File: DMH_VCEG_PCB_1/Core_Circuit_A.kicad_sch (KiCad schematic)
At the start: 106 parts, among them J21 Conn_01x10_PinHeader, J22 Conn_01x10_PinHeader, J24 Conn_01x06_PinHeader, Q1 BC558, Q10 BC548, Q2 BC558, Q3 BC548, Q4 BC548, Q5 MMBFJ113, Q6 MMBFJ113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

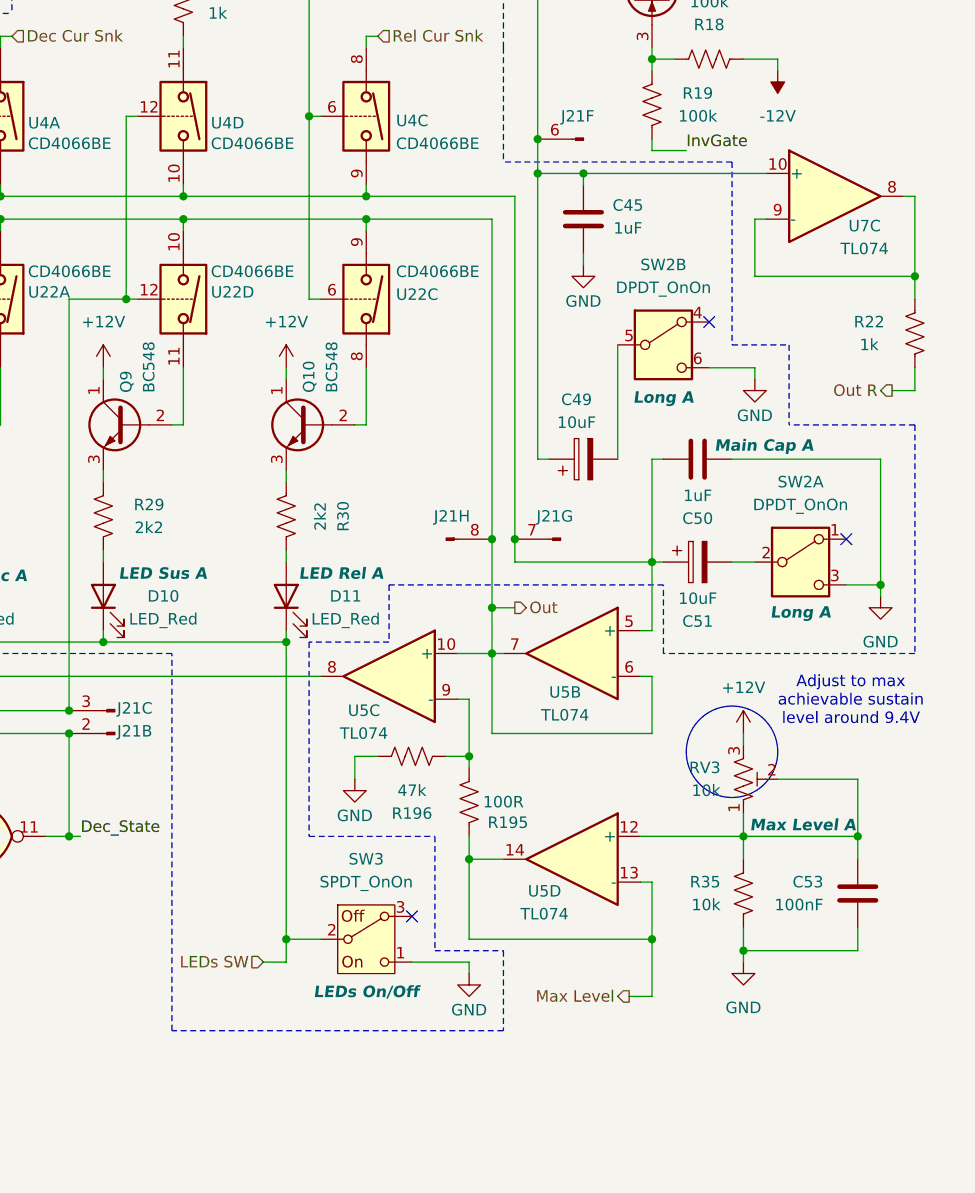
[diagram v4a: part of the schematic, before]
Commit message: Added fast cap selection
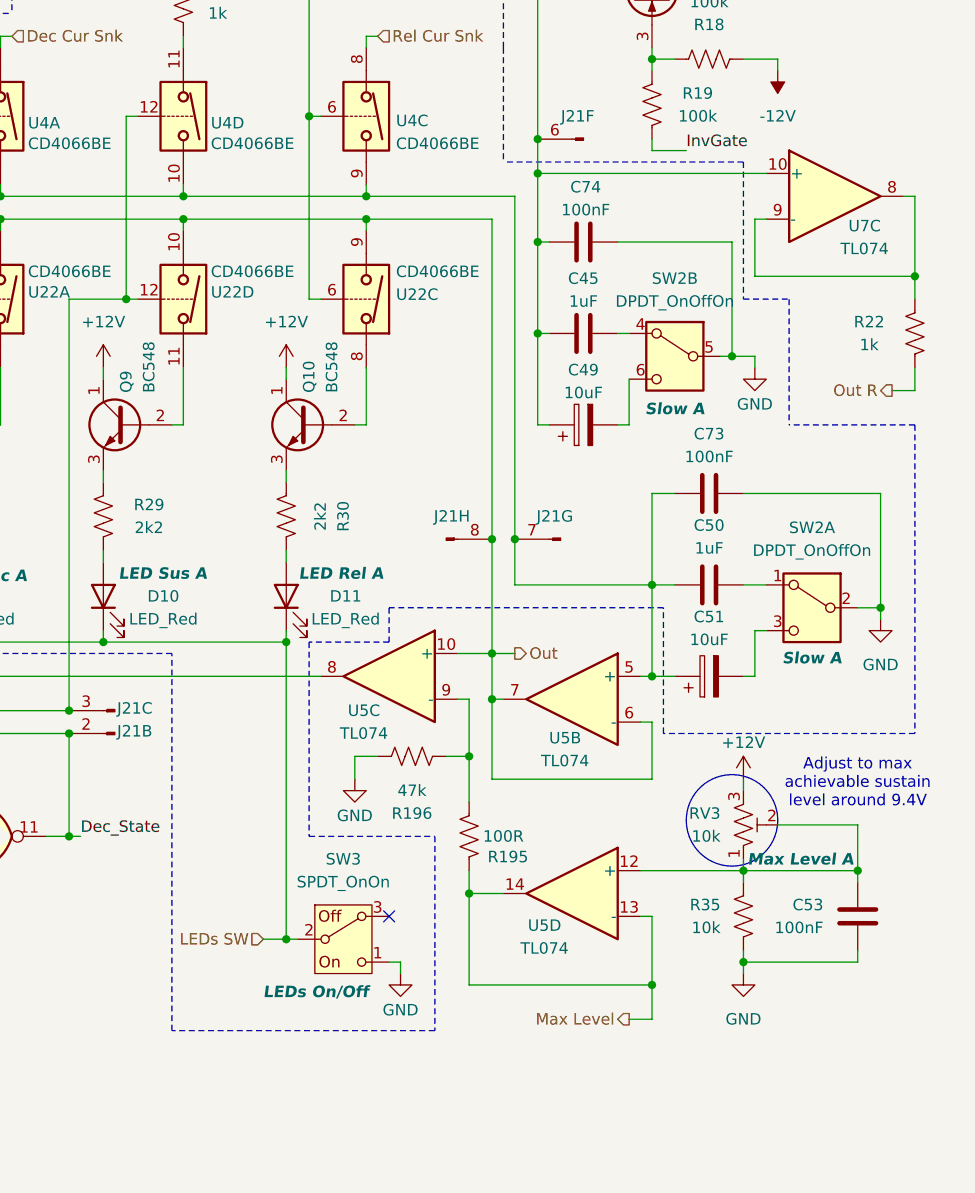
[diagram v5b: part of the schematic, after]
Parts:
- added C73, C74: 100nF, Capacitor_THT:C_Rect_L7.0mm_W4.5mm_P5.00mm, symbol Device:C
- SW2: value DPDT_OnOn -> DPDT_OnOffOn; Function Long A -> Slow A
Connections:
- net GND: now also SW2.2 (B), SW2.5 (B), C73.1, C74.1; no longer C45.1, C50.2, SW2.3 (C), SW2.6 (C)
- net at C45.2, C49.1, J21.6 (Pin_6)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: now also C74.2
- net at C51.1, J21.7 (Pin_7), U4.10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: now also C50.2, C73.2; no longer C50.1
- net at C49.2: now also SW2.6 (C); no longer SW2.5 (B)
- net at C51.2: now also SW2.3 (C); no longer SW2.2 (B)
- net at SW2.4 (A): now also C45.1
- net at SW2.1 (A): now also C50.1
- no-connect marks 5 -> 3
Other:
- moved on the sheet: C45, C49, C50, C51, C53, R195, R35, RV3, SW2A, SW2B, SW3, U5B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

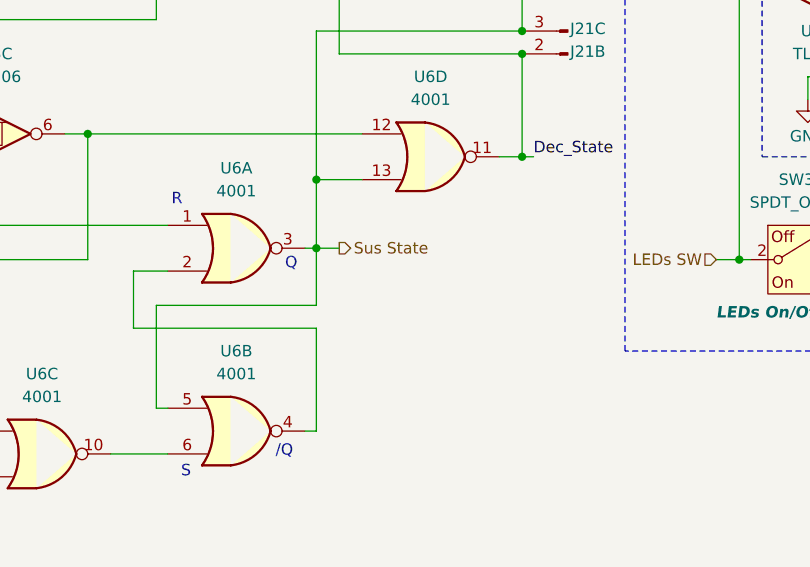
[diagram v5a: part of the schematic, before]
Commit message: Fixed Sus Gate output stage
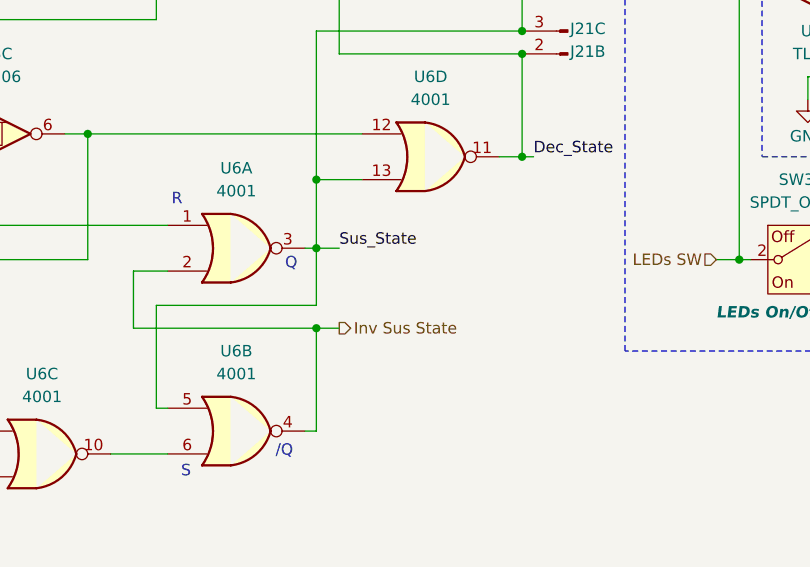
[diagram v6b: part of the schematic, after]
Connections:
- net Inv Sus State: now reaches U6.2, U6.4
- net Sus State renamed Sus_State
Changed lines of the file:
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@@
 	)
 	(junction
+		(at 166.37 162.56)
+		(diameter 0)
+		(color 0 0 0 0)
+	)
+	(junction
 		(at 110.49 86.36)
 		(diameter 0)
@@
 	(wire
 		(pts
+			(xy 166.37 162.56) (xy 168.91 162.56)
+		)
+		(stroke
+			(width 0)
+			(type default)
+		)
+	)
+	(wire
+		(pts
 			(xy 222.25 54.61) (xy 223.52 54.61)
 		)
@@
 		)
 	)
+	(label "Sus_State"
+		(at 168.91 153.67 0)
+		(effects
+			(font
+				(size 1.27 1.27)
+			)
+			(justify left bottom)
+		)
+	)
 	(hierarchical_label "Out R"
 		(shape output)
@@
 		)
 	)
-	(hierarchical_label "Sus State"
-		(shape output)
-		(at 168.91 153.67 0)
-		(effects
-			(font
-				(size 1.27 1.27)
-			)
-			(justify left)
-		)
-	)
 	(hierarchical_label "Att Cur Src"
 		(shape input)
@@
 		(effects
 			(font
+				(size 1.27 1.27)
+			)
+			(justify left)
+		)
+	)
+	(hierarchical_label "Inv Sus State"
+		(shape output)
+		(at 168.91 162.56 0)
+		(effects
+			(font

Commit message: Modified Out R
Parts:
- removed Q5, Q6: MMBFJ113, Package_TO_SOT_THT:TO-92L_Inline, symbol Transistor_FET:MMBFJ113
- removed R11, R18, R19: 100k, Resistor_THT:R_Axial_DIN0207_L6.3mm_D2.5mm_P7.62mm_Horizontal, symbol Device:R_US
- added Q5, Q6: BS170, Package_TO_SOT_THT:TO-92_Inline, symbol Transistor_FET:BS170
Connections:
- net InvGate: now also Q6.2 (G)
- net ProcGate: now also C46.1, D3.1 (K), D5.1 (K), J24.2 (Pin_2), R24.2, SW1.3 (C), U3.1, Q5.2 (G); no longer C48.2, D5.2 (A), R23.1, U1.1
- net at C45.2, C49.1, C74.2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: now also Q5.1 (D), Q6.1 (D)
- net at Q4.1 (C): now also Q6.3 (S)
- net at Q2.1 (C): now also Q5.3 (S)
- new net: C48.2, D5.2 (A), R23.1, U1.1

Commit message: Synced changes to Circuit B
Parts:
- C43: value 1nF -> 10nF
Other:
- note removed: "Was 10n"
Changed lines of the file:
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@@
 		(comment 1 "PCB for 15cm Kosmo format synthesizer module")
 	)
-	(circle
-		(center 70.612 44.196)
-		(radius 3.81)
-		(stroke
-			(width 0)
-			(type default)
-		)
-		(fill
-			(type none)
-		)
-	)
 	(rectangle
 		(start 62.23 125.73)
@@
 		)
 	)
-	(text "Was 10n"
-		(exclude_from_sim no)
-		(at 71.12 49.53 0)
-		(effects
-			(font
-				(size 1.27 1.27)
-			)
-		)
-	)
 	(text "/Q"
 		(exclude_from_sim no)
@@
 	)
 	(junction
+		(at 59.69 107.95)
+		(diameter 0)
+		(color 0 0 0 0)
+	)
+	(junction
 		(at 248.92 19.05)
 		(diameter 0)
@@
 	)
 	(junction
-		(at 59.69 104.14)
-		(diameter 0)
-		(color 0 0 0 0)
-	)
-	(junction
 		(at 222.25 74.93)
 		(diameter 0)
@@
 	(wire
 		(pts
-			(xy 59.69 107.95) (xy 59.69 104.14)
-		)
-		(stroke
-			(width 0)
-			(type default)
-		)
-	)
-	(wire
-		(pts
 			(xy 49.53 26.67) (xy 54.61 26.67)
 		)
@@
 	(wire
 		(pts
-			(xy 59.69 86.36) (xy 59.69 104.14)
-		)
-		(stroke
-			(width 0)
-			(type default)
-		)
-	)
-	(wire
-		(pts
 			(xy 120.65 140.97) (xy 123.19 140.97)
 		)
@@
 	(wire
 		(pts
-			(xy 59.69 104.14) (xy 78.74 104.14)
+			(xy 59.69 107.95) (xy 78.74 107.95)
 		)
 		(stroke
@@
 	(wire
 		(pts
-			(xy 78.74 123.19) (xy 78.74 104.14)
+			(xy 78.74 123.19) (xy 78.74 107.95)
 		)
 		(stroke
@@
 	(wire
 		(pts
+			(xy 59.69 86.36) (xy 59.69 107.95)
+		)
+		(stroke
+			(width 0)
+			(type default)
+		)
+	)
+	(wire
+		(pts
 			(xy 182.88 54.61) (xy 181.61 54.61)
 		)
@@
 			)
 		)
-		(property "Value" "1nF"
+		(property "Value" "10nF"
 			(at 69.85 43.18 90)
 			(effects
